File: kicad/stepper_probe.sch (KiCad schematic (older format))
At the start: 49 parts, among them J1 Conn_01x04_Male, J2 Conn_01x04_Male, J3 BAT, J4 Serial Port, J5 SWD, J6 Reset header, M1 Motor, Q1 PJA3439, SW1 SW_Push, U1 CC6920BSO-5A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

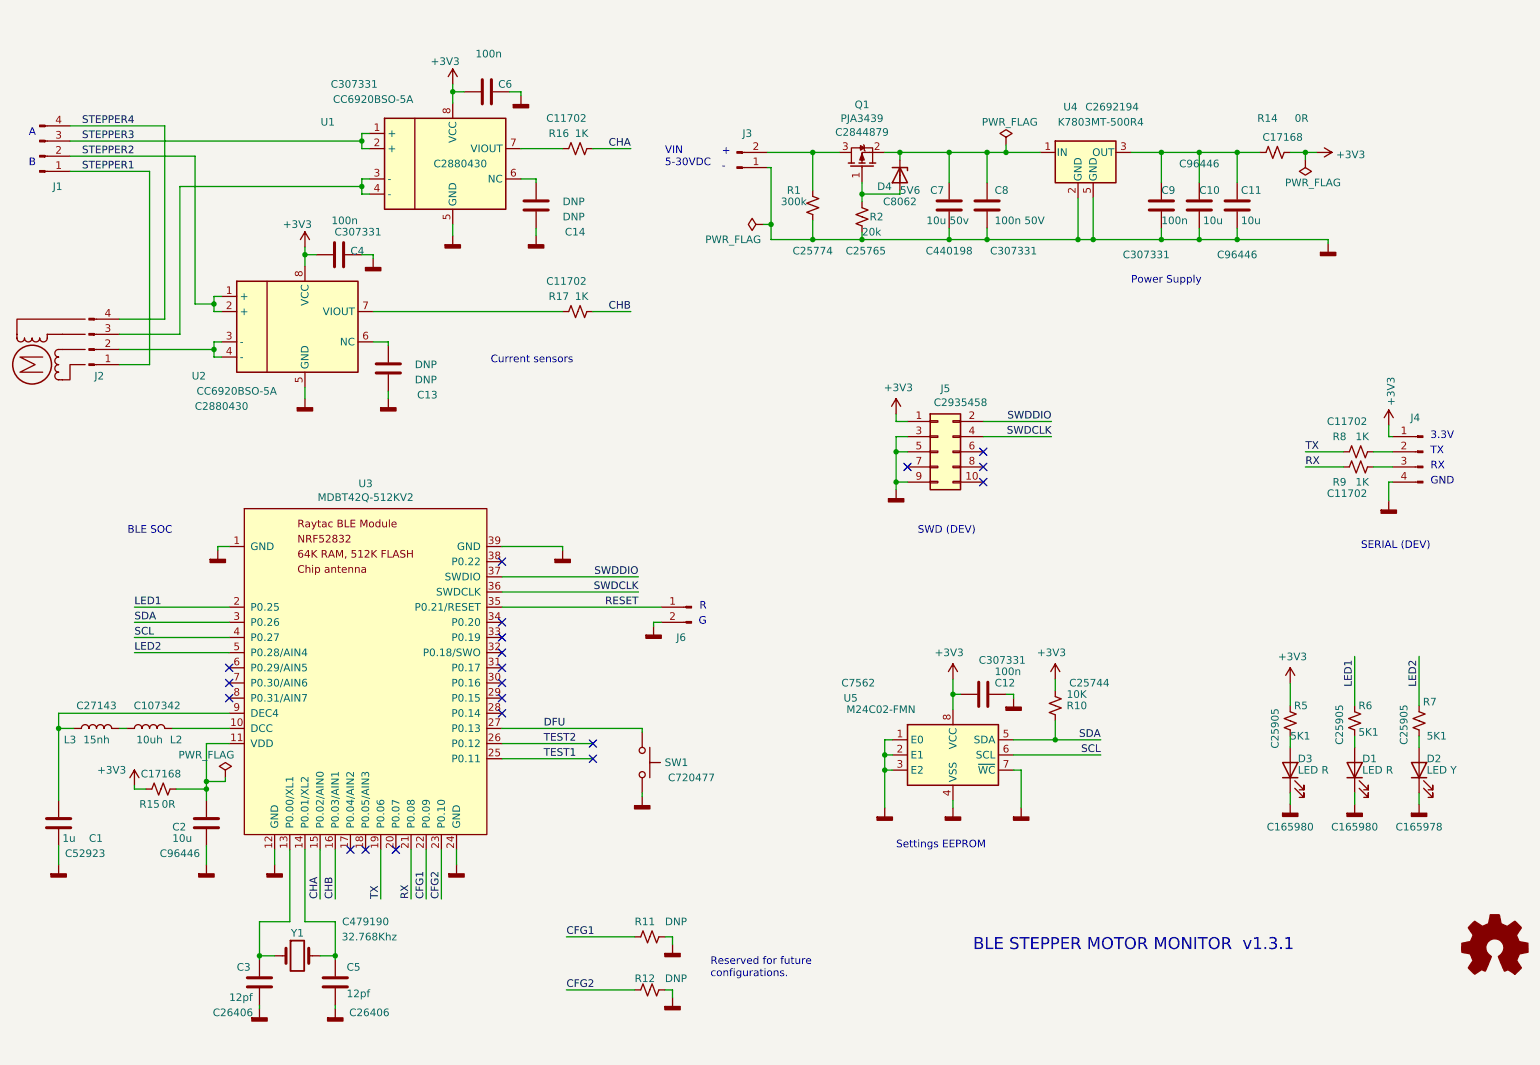
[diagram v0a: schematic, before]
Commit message: Added sensors selection logic. Tweaked the python client.
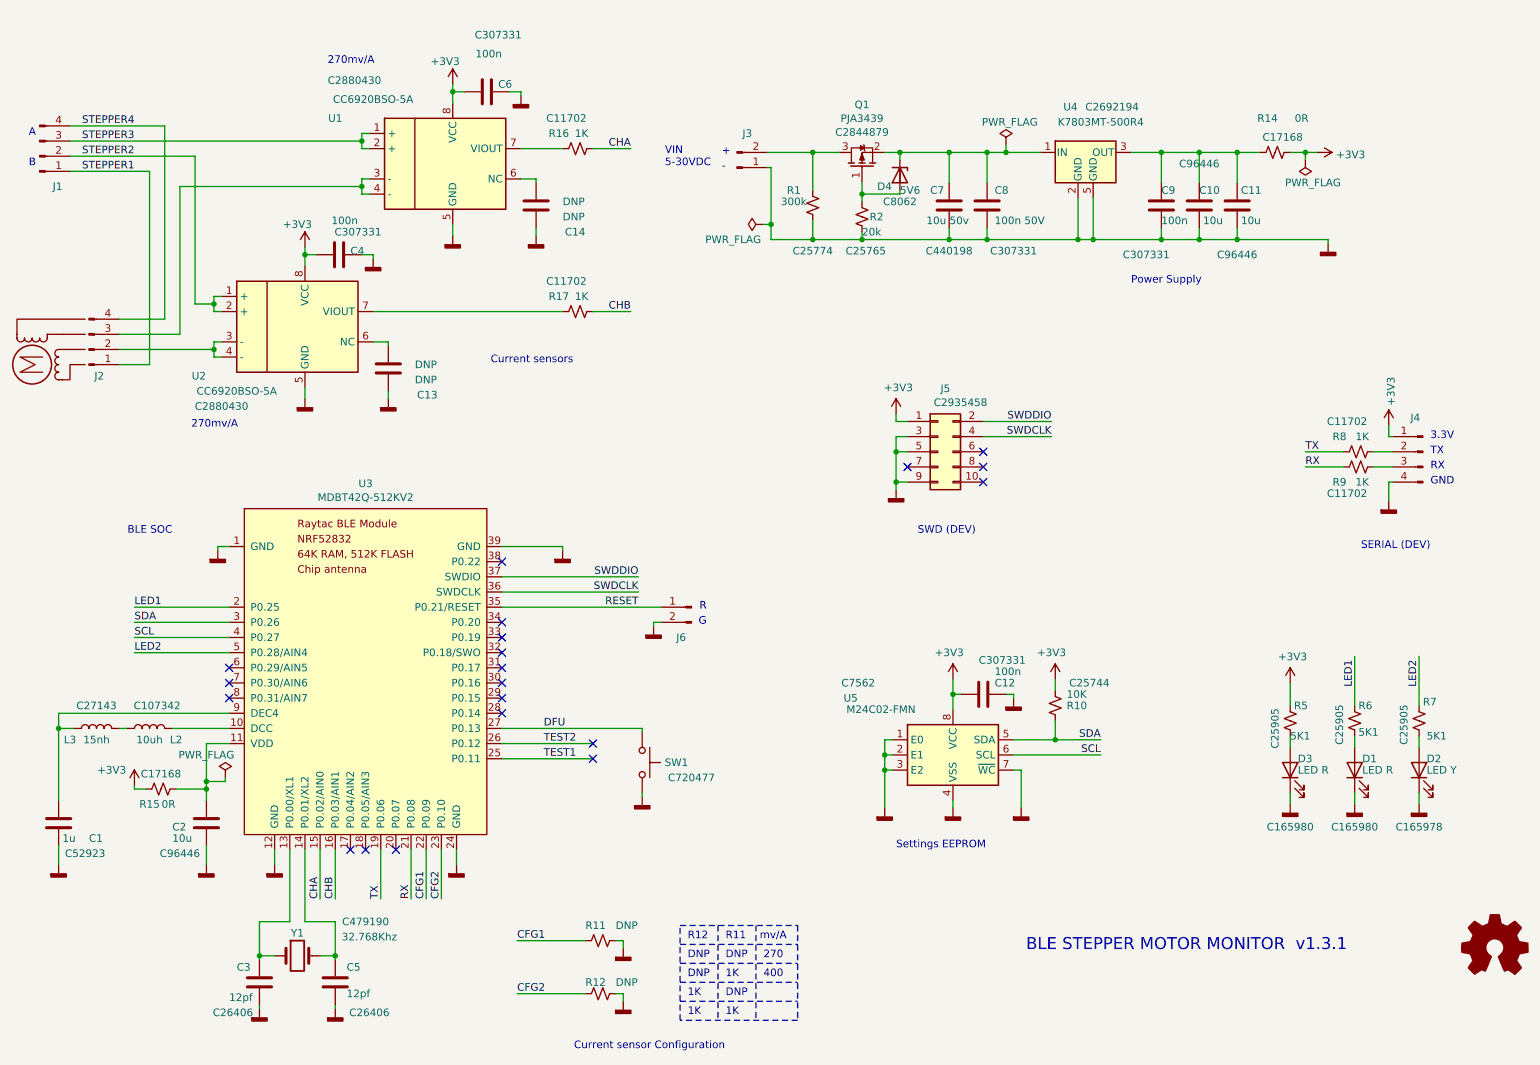
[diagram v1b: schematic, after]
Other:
- note added: "1K"
- note added: "270"
- note added: "270mv/A"
- note added: "400"
- note added: "Current sensor Configuration"
- note added: "DNP"
- note added: "R11"
- note added: "R12"
- note added: "mv/A"
- note removed: "Reserved for future\nconfigurations."
- moved on the sheet: R11, R12
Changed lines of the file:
@@
 U 1 1 627A85BB
 P 3725 1700
-F 0 "U1" H 2850 1975 50  0000 C CNN
+F 0 "U1" H 2900 2000 50  0000 C CNN
 F 1 "CC6920BSO-5A" H 3150 2125 50  0000 C CNN
 F 2 "stepper_probe:SOIC-8_LCPCB_ROT" H 4125 1650 50  0001 L CIN
 F 3 "" H 3725 1700 50  0001 C CNN
-F 4 "C2880430" H 3725 1700 50  0000 C CNN "LCSC"
+F 4 "C2880430" H 2850 2250 50  0000 L CNN "LCSC"
 	1    3725 1700
 	1    0    0    -1
@@
 	1    0    0    -1
 $EndComp
-Text Notes 9225 6900 2    79   ~ 0
+Text Notes 9575 6900 2    79   ~ 0
 BLE STEPPER MOTOR MONITOR  v1.3.1
 $Comp
@@
 F 2 "stepper_probe:C_0402_1005Metric_Pad0.74x0.62mm_HandSolder" H 3938 1075 50  0001 C CNN
 F 3 "~" H 3900 1225 50  0001 C CNN
-F 4 "C307331" V 3850 350 50  0000 C CNN "LCSC"
+F 4 "C307331" V 3525 1300 50  0000 C CNN "LCSC"
 	1    3900 1225
 	0    1    1    0
@@
 L stepper_probe:GND #PWR0111
 U 1 1 62EFA692
-P 5125 7200
-F 0 "#PWR0111" H 5125 6950 50  0001 C CNN
-F 1 "GND" H 5129 7045 50  0001 C CNN
-F 2 "" H 5125 7200 50  0001 C CNN
-F 3 "" H 5125 7200 50  0001 C CNN
-	1    5125 7200
+P 4800 7225
+F 0 "#PWR0111" H 4800 6975 50  0001 C CNN
+F 1 "GND" H 4804 7070 50  0001 C CNN
+F 2 "" H 4800 7225 50  0001 C CNN
+F 3 "" H 4800 7225 50  0001 C CNN
+	1    4800 7225
 	1    0    0    -1
 $EndComp
@@
 L stepper_probe:GND #PWR0112
 U 1 1 62EFAB50
-P 5125 6850
-F 0 "#PWR0112" H 5125 6600 50  0001 C CNN
-F 1 "GND" H 5129 6695 50  0001 C CNN
-F 2 "" H 5125 6850 50  0001 C CNN
-F 3 "" H 5125 6850 50  0001 C CNN
-	1    5125 6850
+P 4800 6875
+F 0 "#PWR0112" H 4800 6625 50  0001 C CNN
+F 1 "GND" H 4804 6720 50  0001 C CNN
+F 2 "" H 4800 6875 50  0001 C CNN
+F 3 "" H 4800 6875 50  0001 C CNN
+	1    4800 6875
 	1    0    0    -1
 $EndComp
@@
 L Device:R_Small_US R11
 U 1 1 62EFB038
-P 4975 6800
-F 0 "R11" V 5075 6900 50  0000 R CNN
-F 1 "DNP" V 5075 6700 50  0000 R CNN
-F 2 "stepper_probe:R_0402_1005Metric_Pad0.72x0.64mm_HandSolder" H 4975 6800 50  0001 C CNN
-F 3 "~" H 4975 6800 50  0001 C CNN
-F 4 "DNP" H 4975 6800 50  0001 C CNN "LCSC"
-	1    4975 6800
+P 4650 6825
+F 0 "R11" V 4750 6925 50  0000 R CNN
+F 1 "DNP" V 4750 6725 50  0000 R CNN
+F 2 "stepper_probe:R_0402_1005Metric_Pad0.72x0.64mm_HandSolder" H 4650 6825 50  0001 C CNN
+F 3 "~" H 4650 6825 50  0001 C CNN
+F 4 "DNP" H 4650 6825 50  0001 C CNN "LCSC"
+	1    4650 6825
 	0    -1   -1   0
 $EndComp
@@
 L Device:R_Small_US R12
 U 1 1 62EFBB37
-P 4975 7150
-F 0 "R12" V 5050 7250 50  0000 R CNN
-F 1 "DNP" V 5050 7050 50  0000 R CNN
-F 2 "stepper_probe:R_0402_1005Metric_Pad0.72x0.64mm_HandSolder" H 4975 7150 50  0001 C CNN
-F 3 "~" H 4975 7150 50  0001 C CNN
-F 4 "DNP" H 4975 7150 50  0001 C CNN "LCSC"
-	1    4975 7150
+P 4650 7175
+F 0 "R12" V 4725 7275 50  0000 R CNN
+F 1 "DNP" V 4725 7075 50  0000 R CNN
+F 2 "stepper_probe:R_0402_1005Metric_Pad0.72x0.64mm_HandSolder" H 4650 7175 50  0001 C CNN
+F 3 "~" H 4650 7175 50  0001 C CNN
+F 4 "DNP" H 4650 7175 50  0001 C CNN "LCSC"
+	1    4650 7175
 	0    -1   -1   0
 $EndComp
 Wire Wire Line
-	5075 6800 5125 6800
-Wire Wire Line
-	5125 6800 5125 6850
-Wire Wire Line
-	5075 7150 5125 7150
-Wire Wire Line
-	5125 7150 5125 7200
-Text Label 4425 6800 0    50   ~ 0
+	4750 6825 4800 6825
+Wire Wire Line
+	4800 6825 4800 6875
+Wire Wire Line
+	4750 7175 4800 7175
+Wire Wire Line
+	4800 7175 4800 7225
+Text Label 4100 6825 0    50   ~ 0
 CFG1
 Wire Wire Line
-	4425 6800 4875 6800
-Wire Wire Line
-	4425 7150 4875 7150
-Text Label 4425 7150 0    50   ~ 0
+	4100 6825 4550 6825
+Wire Wire Line
+	4100 7175 4550 7175
+Text Label 4100 7175 0    50   ~ 0
 CFG2
 Wire Wire Line
@@
 Text Label 3600 6550 1    50   ~ 0
 CFG2
-Text Notes 5375 7075 0    50   ~ 0
-Reserved for future\nconfigurations.
 Text Notes 3925 3025 0    50   ~ 0
 Current sensors
@@
 Wire Wire Line
 	6375 1900 6375 1825
+Text Notes 5475 7075 0    50   ~ 0
+1K
+Text Notes 5225 6950 0    50   ~ 0
+DNP
+Text Notes 5475 6950 0    50   ~ 0
+DNP
+Text Notes 5225 7075 0    50   ~ 0
+DNP
+Text Notes 5225 7200 0    50   ~ 0
+1K
+Text Notes 5475 7200 0    50   ~ 0
+DNP
+Text Notes 5475 7325 0    50   ~ 0
+1K
+Text Notes 5225 7325 0    50   ~ 0
+1K
+Text Notes 5725 7075 0    50   ~ 0
+400
+Text Notes 5700 6825 0    50   ~ 0
+mv/A
+Text Notes 5725 6950 0    50   ~ 0
+270
+Text Notes 5475 6825 0    50   ~ 0
+R11
+Text Notes 5225 6825 0    50   ~ 0
+R12
+Wire Notes Line width 4 style solid
+	5950 6725 5950 7350
+Wire Notes Line width 4 style solid
+	5950 7350 5175 7350
+Wire Notes Line width 4 style solid
+	5175 7350 5175 6725
+Wire Notes Line width 4 style solid
+	5175 6725 5950 6725
+Wire Notes Line width 4 style solid
+	5175 6850 5950 6850
+Wire Notes Line width 4 style solid
+	5175 6975 5950 6975
+Wire Notes Line width 4 style solid
+	5175 7100 5950 7100
+Wire Notes Line width 4 style solid
+	5175 7225 5950 7225
+Wire Notes Line width 4 style solid
+	5425 6725 5425 7350
+Wire Notes Line width 4 style solid
+	5675 6725 5675 7350
+Text Notes 4475 7550 0    50   ~ 0
+Current sensor Configuration
+Text Notes 2850 1050 0    50   ~ 0
+270mv/A
+Text Notes 1950 3450 0    50   ~ 0
+270mv/A
 $EndSCHEMATC

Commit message: Tweaks
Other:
- note added: "For an external antenna, replace\nwith MDBT42Q-U512KV2"
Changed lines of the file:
@@
 U 1 1 62C25ED4
 P 3100 4625
-F 0 "U3" H 3100 5440 50  0000 C CNN
-F 1 "MDBT42Q-512KV2" H 3100 5349 50  0000 C CNN
+F 0 "U3" H 2425 5425 50  0000 C CNN
+F 1 "MDBT42Q-512KV2" H 2725 5350 50  0000 C CNN
 F 2 "stepper_probe:RAYTAC_MDBT42Q" H 3100 4625 50  0001 C CNN
 F 3 "" H 3100 4625 50  0001 C CNN
@@
 Text Notes 1950 3450 0    50   ~ 0
 270mv/A
+Text Notes 3325 3925 0    50   ~ 0
+For an external antenna, replace\nwith MDBT42Q-U512KV2
 $EndSCHEMATC

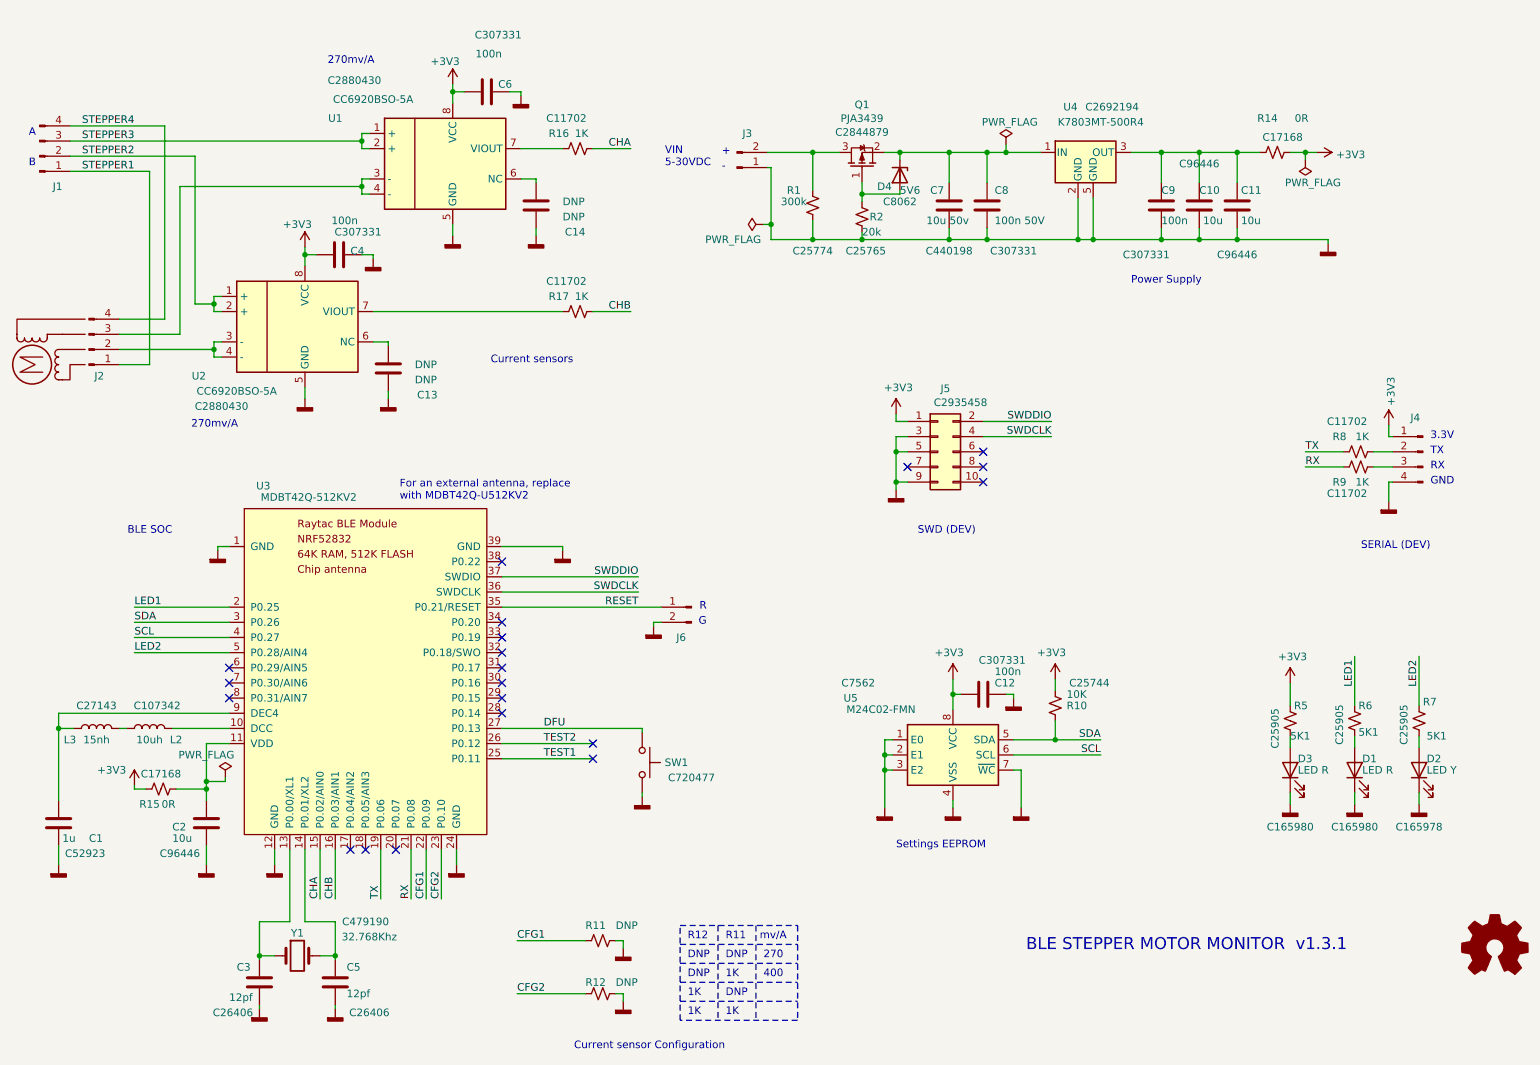
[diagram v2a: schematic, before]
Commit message: Now using average for zero calibration. Also updated README and Kicad.
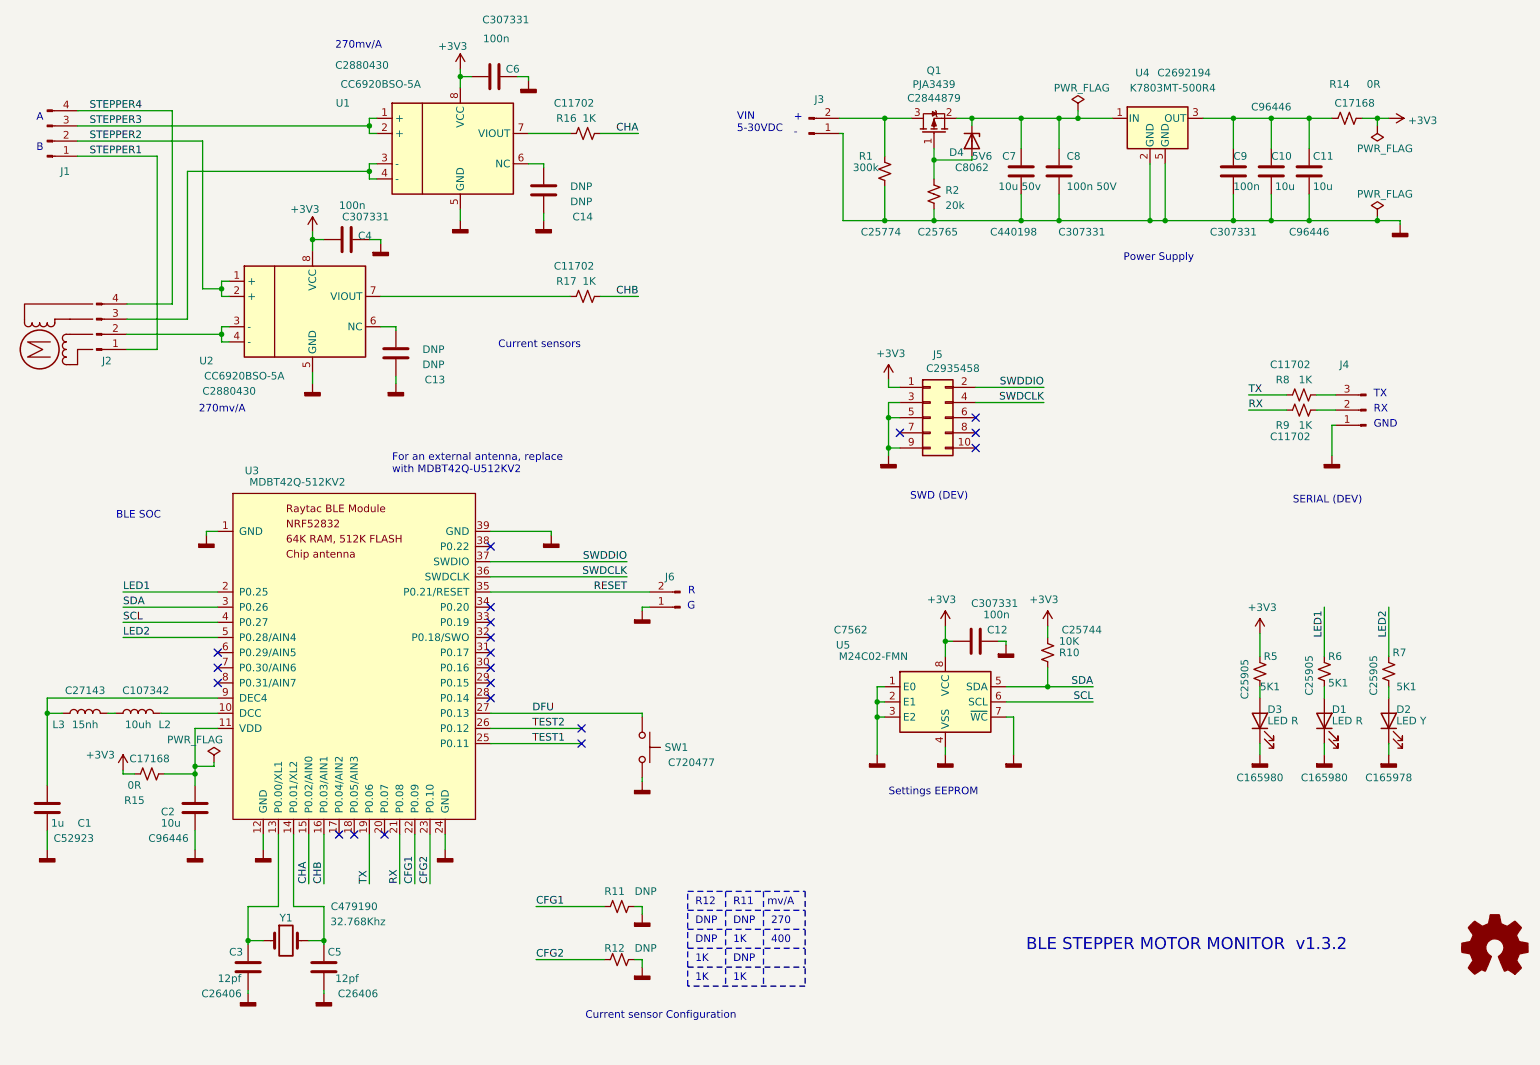
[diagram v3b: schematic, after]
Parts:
- removed J4: Serial Port, stepper_probe:PinHeader_1x04_P2.54mm_Vertical, symbol Connector:Conn_01x04_Male
- added J4: Conn_01x03_Male, stepper_probe:PinHeader_1x03_P2.54mm_Vertical, symbol Connector:Conn_01x03_Male
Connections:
- net GND: now also J6.1 (Pin_1), J4.1 (Pin_1); no longer J6.2 (Pin_2)
- net RESET: now also J6.2 (Pin_2); no longer J6.1 (Pin_1)
- net at R8.1: now also J4.3 (Pin_3)
- net at R9.1: now also J4.2 (Pin_2)
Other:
- note added: "BLE STEPPER MOTOR MONITOR v1.3.2"
- note removed: "3.3V\n"
- note removed: "BLE STEPPER MOTOR MONITOR v1.3.1"
- moved on the sheet: C1, C10, C11, C12, C13, C14, C2, C3, C4, C5, C6, C7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

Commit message: Flushing open files.
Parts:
- J4: LCSC (none) -> C49257
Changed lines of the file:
@@
 F 2 "stepper_probe:PinHeader_1x03_P2.54mm_Vertical" H 9700 3325 50  0001 C CNN
 F 3 "~" H 9700 3325 50  0001 C CNN
+F 4 "C49257" H 9700 3325 50  0001 C CNN "LCSC"
 	1    9700 3325
 	-1   0    0    1
